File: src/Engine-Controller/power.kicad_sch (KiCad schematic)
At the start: 49 parts, among them P1 EJ508A, P18 PPTC041LFBN-RC, P7 647676-2, U10 LMS8117AMP-3.3_NOPB, U2 LM22672MRE-5.0_NOPB, U3 LMS8117AMP-3.3_NOPB, U6 TPS2115APWR

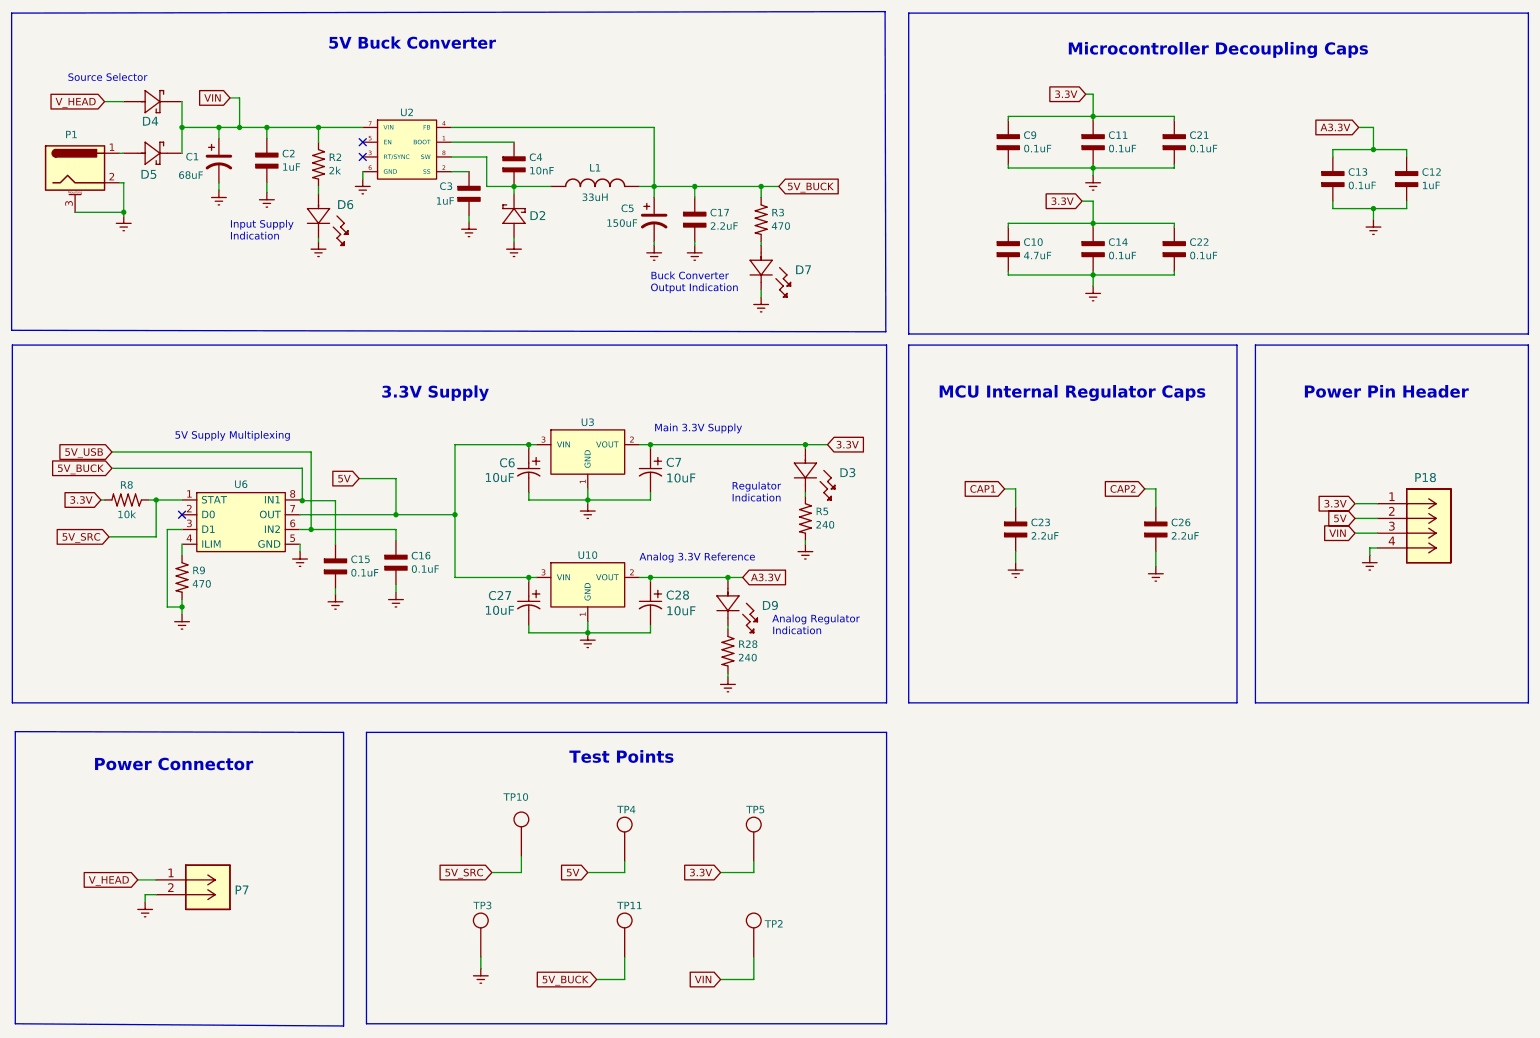
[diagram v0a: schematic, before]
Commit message: copied over 5.0/5.1 updates from Gain-Calc branch
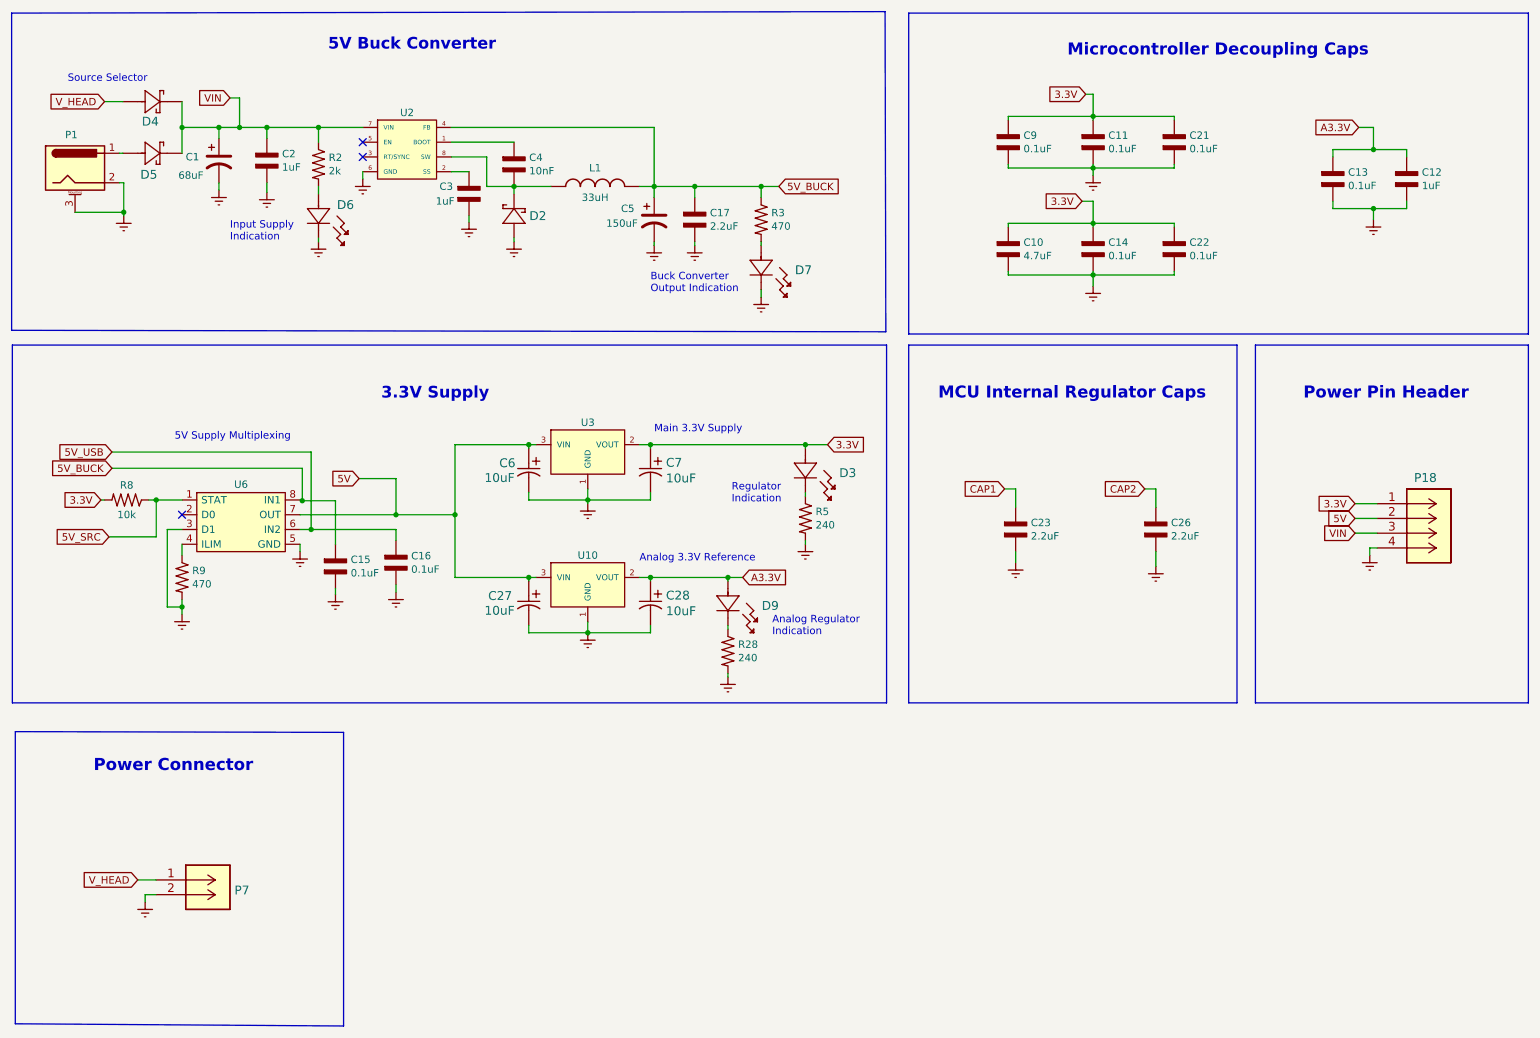
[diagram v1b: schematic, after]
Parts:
- removed TP10, TP11: TP, Engine-Controller:TP, symbol Engine-Controller:TP
- removed TP2: TPVIN, Engine-Controller:TP, symbol Engine-Controller:TP
- removed TP3: TPGND, Engine-Controller:TP, symbol Engine-Controller:TP
- removed TP4: TP5V, Engine-Controller:TP, symbol Engine-Controller:TP
- removed TP5: 3.3V, Engine-Controller:TP, symbol Engine-Controller:TP
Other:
- note removed: "Test Points"
